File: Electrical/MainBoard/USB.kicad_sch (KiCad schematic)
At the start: 0 parts

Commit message: Add more schematics and begin floorplanning
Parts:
- added C10: 0.1 uF, Capacitor_SMD:C_0805_2012Metric_Pad1.18x1.45mm_HandSolder, symbol Device:C
- added D2 (x2): LED, LED_SMD:LED_0805_2012Metric_Pad1.15x1.40mm_HandSolder, symbol Device:LED
- added J13: USB_B_Micro, RobotLibrary:AMPHENOL_10118193-0001LF, symbol Connector:USB_B_Micro
- added R4 (x2): 130R, Resistor_SMD:R_0805_2012Metric_Pad1.20x1.40mm_HandSolder, symbol Device:R_US
- added U10: MCP2221A-I_SL, RobotLibrary:SOIC127P600X175-14N, symbol RobotLibary:MCP2221A-I_SL
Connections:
- new net: J13.2 (D-), U10.12 (D-)
- new net: J13.3 (D+), U10.13 (D+)
- new net: D2.1 (K), U10.2 (GP0)
- new net: D2.1 (K), U10.3 (GP1)
- new net: D2.2 (A), R4.2 (x2)
- new net +3.3V: C10.1, R4.1, R4.1, U10.1 (VDD), U10.11 (VUSB)
- new net GND: C10.2, J13.5 (GND), U10.14 (VSS)
- new net U1RX: U10.6 (UTX)
- new net U1TX: U10.5 (URX)
- new net USB Reset: U10.4 (~{RST})
- no-connect marks 0 -> 6
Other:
- note added: "RX Indicator"
- note added: "TX Indicator"

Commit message: Begin layout of pcb
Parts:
- renumbered U10 to U9
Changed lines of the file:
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@@
   (symbol (lib_id "power:GND") (at 173.355 135.89 0) (unit 1)
     (in_bom yes) (on_board yes) (dnp no) (fields_autoplaced)
-    (property "Reference" "#PWR0108" (at 173.355 142.24 0)
+    (property "Reference" "#PWR097" (at 173.355 142.24 0)
       (effects (font (size 1.27 1.27)) hide)
     )
@@
       (project "MainBoard"
         (path "/bd24c4db-4e36-4117-bd4f-5228ef241da9/f45a9536-5513-41e8-a632-51113262766c"
-          (reference "#PWR0108") (unit 1)
+          (reference "#PWR097") (unit 1)
         )
       )
@@
   (symbol (lib_id "power:GND") (at 238.125 136.525 0) (unit 1)
     (in_bom yes) (on_board yes) (dnp no) (fields_autoplaced)
-    (property "Reference" "#PWR0107" (at 238.125 142.875 0)
+    (property "Reference" "#PWR098" (at 238.125 142.875 0)
       (effects (font (size 1.27 1.27)) hide)
     )
@@
       (project "MainBoard"
         (path "/bd24c4db-4e36-4117-bd4f-5228ef241da9/f45a9536-5513-41e8-a632-51113262766c"
-          (reference "#PWR0107") (unit 1)
+          (reference "#PWR098") (unit 1)
         )
       )
@@
   (symbol (lib_id "power:GND") (at 247.015 104.14 0) (unit 1)
     (in_bom yes) (on_board yes) (dnp no)
-    (property "Reference" "#PWR0109" (at 247.015 110.49 0)
+    (property "Reference" "#PWR0100" (at 247.015 110.49 0)
       (effects (font (size 1.27 1.27)) hide)
     )
@@
       (project "MainBoard"
         (path "/bd24c4db-4e36-4117-bd4f-5228ef241da9/f45a9536-5513-41e8-a632-51113262766c"
-          (reference "#PWR0109") (unit 1)
+          (reference "#PWR0100") (unit 1)
         )
       )
@@
   (symbol (lib_id "RobotLibary:MCP2221A-I_SL") (at 222.885 121.285 0) (unit 1)
     (in_bom yes) (on_board yes) (dnp no) (fields_autoplaced)
-    (property "Reference" "U10" (at 222.885 99.06 0)
+    (property "Reference" "U9" (at 222.885 99.06 0)
       (effects (font (size 1.27 1.27)))
     )
@@
       (project "MainBoard"
         (path "/bd24c4db-4e36-4117-bd4f-5228ef241da9/f45a9536-5513-41e8-a632-51113262766c"
-          (reference "U10") (unit 1)
+          (reference "U9") (unit 1)
         )
       )
@@
   (symbol (lib_id "power:+3.3V") (at 273.05 114.3 0) (unit 1)
     (in_bom yes) (on_board yes) (dnp no) (fields_autoplaced)
-    (property "Reference" "#PWR0111" (at 273.05 118.11 0)
+    (property "Reference" "#PWR0101" (at 273.05 118.11 0)
       (effects (font (size 1.27 1.27)) hide)
     )
@@
       (project "MainBoard"
         (path "/bd24c4db-4e36-4117-bd4f-5228ef241da9/f45a9536-5513-41e8-a632-51113262766c"
-          (reference "#PWR0111") (unit 1)
+          (reference "#PWR0101") (unit 1)
         )
       )
@@
         )
         (path "/bd24c4db-4e36-4117-bd4f-5228ef241da9/f45a9536-5513-41e8-a632-51113262766c"
-          (reference "R25") (unit 1)
+          (reference "R15") (unit 1)
         )
       )
@@
   (symbol (lib_id "power:+3.3V") (at 288.925 237.49 0) (unit 1)
     (in_bom yes) (on_board yes) (dnp no) (fields_autoplaced)
-    (property "Reference" "#PWR048" (at 288.925 241.3 0)
+    (property "Reference" "#PWR0103" (at 288.925 241.3 0)
       (effects (font (size 1.27 1.27)) hide)
     )
@@
       (project "MainBoard"
         (path "/bd24c4db-4e36-4117-bd4f-5228ef241da9/f45a9536-5513-41e8-a632-51113262766c"
-          (reference "#PWR048") (unit 1)
+          (reference "#PWR0103") (unit 1)
         )
       )
@@
   (symbol (lib_id "power:+3.3V") (at 247.015 94.615 0) (unit 1)
     (in_bom yes) (on_board yes) (dnp no) (fields_autoplaced)
-    (property "Reference" "#PWR0110" (at 247.015 98.425 0)
+    (property "Reference" "#PWR099" (at 247.015 98.425 0)
       (effects (font (size 1.27 1.27)) hide)
     )
@@
       (project "MainBoard"
         (path "/bd24c4db-4e36-4117-bd4f-5228ef241da9/f45a9536-5513-41e8-a632-51113262766c"
-          (reference "#PWR0110") (unit 1)
+          (reference "#PWR099") (unit 1)
         )
       )
@@
   (symbol (lib_id "power:GND") (at 285.115 254.635 0) (unit 1)
     (in_bom yes) (on_board yes) (dnp no) (fields_autoplaced)
-    (property "Reference" "#PWR0106" (at 285.115 260.985 0)
+    (property "Reference" "#PWR0102" (at 285.115 260.985 0)
       (effects (font (size 1.27 1.27)) hide)
     )
@@
       (project "MainBoard"
         (path "/bd24c4db-4e36-4117-bd4f-5228ef241da9/f45a9536-5513-41e8-a632-51113262766c"
-          (reference "#PWR0106") (unit 1)
+          (reference "#PWR0102") (unit 1)
         )
       )
@@
         )
         (path "/bd24c4db-4e36-4117-bd4f-5228ef241da9/f45a9536-5513-41e8-a632-51113262766c"
-          (reference "C20") (unit 1)
+          (reference "C19") (unit 1)
         )
       )
@@
         )
         (path "/bd24c4db-4e36-4117-bd4f-5228ef241da9/f45a9536-5513-41e8-a632-51113262766c"
-          (reference "R26") (unit 1)
+          (reference "R16") (unit 1)
         )
       )
@@
         )
         (path "/bd24c4db-4e36-4117-bd4f-5228ef241da9/f45a9536-5513-41e8-a632-51113262766c"
-          (reference "J15") (unit 1)
-        )
-      )
+          (reference "J9") (unit 1)
+        )
+      )

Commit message: Add some finishing touches and create preliminary boms
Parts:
- removed D2 (x2): LED, LED_SMD:LED_0805_2012Metric_Pad1.15x1.40mm_HandSolder, symbol Device:LED
- added D1 (x2): LED, LED_SMD:LED_0805_2012Metric_Pad1.15x1.40mm_HandSolder, symbol Device:LED
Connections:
- net at U9.2 (GP0): now also D1.1 (K)
- net at U9.3 (GP1): now also D1.1 (K)
- net at R4.2: now also D1.2 (A) (x2)
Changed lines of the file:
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@@
-    )
-  )
-  (symbol (lib_id "Device:LED") (at 257.81 123.825 0) (unit 1)
-    (in_bom yes) (on_board yes) (dnp no)
-    (property "Reference" "D2" (at 259.08 126.365 0)
-      (effects (font (size 1.27 1.27)) (justify right))
-    )
-    (property "Value" "LED" (at 259.715 128.27 0)
-      (effects (font (size 1.27 1.27)) (justify right))
-    )
-    (property "Footprint" "LED_SMD:LED_0805_2012Metric_Pad1.15x1.40mm_HandSolder" (at 257.81 123.825 0)
-      (effects (font (size 1.27 1.27)) hide)
-    )
-    (property "Datasheet" "https://www.we-online.com/katalog/datasheet/150080RS75000.pdf" (at 257.81 123.825 0)
-      (effects (font (size 1.27 1.27)) hide)
-    )
-    (property "Description" "LED GREEN CLEAR 0805 SMD" (at 257.81 123.825 0)
-      (effects (font (size 1.27 1.27)) hide)
-    )
-    (property "Mfr" "Würth Elektronik" (at 257.81 123.825 0)
-      (effects (font (size 1.27 1.27)) hide)
-    )
-    (property "Mfr P/N" "150080VS75000" (at 257.81 123.825 0)
-      (effects (font (size 1.27 1.27)) hide)
-    )
-    (property "Supplier 1" "DigiKey" (at 257.81 123.825 0)
-      (effects (font (size 1.27 1.27)) hide)
-    )
-    (property "Supplier 1 P/N" "732-4986-1-ND" (at 257.81 123.825 0)
-      (effects (font (size 1.27 1.27)) hide)
-    )
-    (property "Supplier 2" "" (at 257.81 123.825 0)
-      (effects (font (size 1.27 1.27)) hide)
-    )
-    (property "Supplier 2 P/N" "" (at 257.81 123.825 0)
-      (effects (font (size 1.27 1.27)) hide)
-    )
-    (pin "1")
-    (pin "2")
-    (instances
-      (project "MainBoard"
-        (path "/bd24c4db-4e36-4117-bd4f-5228ef241da9/783fabe8-20be-46c9-9aa7-e8ec2689d507"
-          (reference "D2") (unit 1)
-        )
-        (path "/bd24c4db-4e36-4117-bd4f-5228ef241da9/f45a9536-5513-41e8-a632-51113262766c"
-          (reference "D9") (unit 1)
-        )
-      )
     )
   )
@@
     )
   )
-  (symbol (lib_id "Device:LED") (at 258.445 120.015 0) (unit 1)
-    (in_bom yes) (on_board yes) (dnp no)
-    (property "Reference" "D2" (at 260.35 115.57 0)
-      (effects (font (size 1.27 1.27)) (justify right))
-    )
-    (property "Value" "LED" (at 260.35 117.475 0)
-      (effects (font (size 1.27 1.27)) (justify right))
-    )
-    (property "Footprint" "LED_SMD:LED_0805_2012Metric_Pad1.15x1.40mm_HandSolder" (at 258.445 120.015 0)
-      (effects (font (size 1.27 1.27)) hide)
-    )
-    (property "Datasheet" "https://www.we-online.com/katalog/datasheet/150080RS75000.pdf" (at 258.445 120.015 0)
-      (effects (font (size 1.27 1.27)) hide)
-    )
-    (property "Description" "LED GREEN CLEAR 0805 SMD" (at 258.445 120.015 0)
-      (effects (font (size 1.27 1.27)) hide)
-    )
-    (property "Mfr" "Würth Elektronik" (at 258.445 120.015 0)
-      (effects (font (size 1.27 1.27)) hide)
-    )
-    (property "Mfr P/N" "150080VS75000" (at 258.445 120.015 0)
-      (effects (font (size 1.27 1.27)) hide)
-    )
-    (property "Supplier 1" "DigiKey" (at 258.445 120.015 0)
-      (effects (font (size 1.27 1.27)) hide)
-    )
-    (property "Supplier 1 P/N" "732-4986-1-ND" (at 258.445 120.015 0)
-      (effects (font (size 1.27 1.27)) hide)
-    )
-    (property "Supplier 2" "" (at 258.445 120.015 0)
-      (effects (font (size 1.27 1.27)) hide)
-    )
-    (property "Supplier 2 P/N" "" (at 258.445 120.015 0)
-      (effects (font (size 1.27 1.27)) hide)
-    )
-    (pin "1")
-    (pin "2")
-    (instances
-      (project "MainBoard"
-        (path "/bd24c4db-4e36-4117-bd4f-5228ef241da9/783fabe8-20be-46c9-9aa7-e8ec2689d507"
-          (reference "D2") (unit 1)
-        )
-        (path "/bd24c4db-4e36-4117-bd4f-5228ef241da9/f45a9536-5513-41e8-a632-51113262766c"
-          (reference "D10") (unit 1)
-        )
-      )
-    )
-  )
   (symbol (lib_id "power:+3.3V") (at 247.015 94.615 0) (unit 1)
     (in_bom yes) (on_board yes) (dnp no) (fields_autoplaced)
@@
         )
       )
+    )
+  )
+  (symbol (lib_id "Device:LED") (at 258.445 120.015 0) (unit 1)
+    (in_bom yes) (on_board yes) (dnp no)
+    (property "Reference" "D1" (at 259.715 116.84 0)
+      (effects (font (size 1.27 1.27)) (justify right))
+    )
+    (property "Value" "LED" (at 259.715 114.935 0)
+      (effects (font (size 1.27 1.27)) (justify right))
+    )
+    (property "Footprint" "LED_SMD:LED_0805_2012Metric_Pad1.15x1.40mm_HandSolder" (at 258.445 120.015 0)
+      (effects (font (size 1.27 1.27)) hide)
+    )
+    (property "Datasheet" "https://www.we-online.com/katalog/datasheet/150080RS75000.pdf" (at 258.445 120.015 0)
+      (effects (font (size 1.27 1.27)) hide)
+    )
+    (property "Description" "LED RED CLEAR 0805 SMD" (at 258.445 120.015 0)
+      (effects (font (size 1.27 1.27)) hide)
+    )
+    (property "Mfr" "Würth Elektronik" (at 258.445 120.015 0)
+      (effects (font (size 1.27 1.27)) hide)
+    )
+    (property "Mfr P/N" "150080RS75000" (at 258.445 120.015 0)
+      (effects (font (size 1.27 1.27)) hide)
+    )
+    (property "Supplier 1" "DigiKey" (at 258.445 120.015 0)
+      (effects (font (size 1.27 1.27)) hide)
+    )
+    (property "Supplier 1 P/N" "732-4984-1-ND" (at 258.445 120.015 0)
+      (effects (font (size 1.27 1.27)) hide)
+    )
+    (property "Supplier 2" "" (at 258.445 120.015 0)
+      (effects (font (size 1.27 1.27)) hide)
+    )
+    (property "Supplier 2 P/N" "" (at 258.445 120.015 0)
+      (effects (font (size 1.27 1.27)) hide)
+    )
+    (pin "1")
+    (pin "2")
+    (instances
+      (project "MainBoard"
+        (path "/bd24c4db-4e36-4117-bd4f-5228ef241da9/783fabe8-20be-46c9-9aa7-e8ec2689d507"
+          (reference "D1") (unit 1)
+        )
+        (path "/bd24c4db-4e36-4117-bd4f-5228ef241da9/8ba935aa-d6da-451b-8954-3c3ef7086bfd"
+          (reference "D1") (unit 1)
+        )
+        (path "/bd24c4db-4e36-4117-bd4f-5228ef241da9/f45a9536-5513-41e8-a632-51113262766c"
+          (reference "D10") (unit 1)
+        )
+      )
+    )
+  )
+  (symbol (lib_id "Device:LED") (at 257.81 123.825 0) (unit 1)
+    (in_bom yes) (on_board yes) (dnp no)
+    (property "Reference" "D1" (at 259.715 128.27 0)
+      (effects (font (size 1.27 1.27)) (justify right))
+    )
+    (property "Value" "LED" (at 259.715 126.365 0)
+      (effects (font (size 1.27 1.27)) (justify right))
+    )
+    (property "Footprint" "LED_SMD:LED_0805_2012Metric_Pad1.15x1.40mm_HandSolder" (at 257.81 123.825 0)
+      (effects (font (size 1.27 1.27)) hide)
+    )
+    (property "Datasheet" "https://www.we-online.com/katalog/datasheet/150080RS75000.pdf" (at 257.81 123.825 0)
+      (effects (font (size 1.27 1.27)) hide)
+    )
+    (property "Description" "LED RED CLEAR 0805 SMD" (at 257.81 123.825 0)
+      (effects (font (size 1.27 1.27)) hide)
+    )
+    (property "Mfr" "Würth Elektronik" (at 257.81 123.825 0)
+      (effects (font (size 1.27 1.27)) hide)
+    )
+    (property "Mfr P/N" "150080RS75000" (at 257.81 123.825 0)
+      (effects (font (size 1.27 1.27)) hide)
+    )
+    (property "Supplier 1" "DigiKey" (at 257.81 123.825 0)
+      (effects (font (size 1.27 1.27)) hide)
+    )
+    (property "Supplier 1 P/N" "732-4984-1-ND" (at 257.81 123.825 0)
+      (effects (font (size 1.27 1.27)) hide)
+    )
+    (property "Supplier 2" "" (at 257.81 123.825 0)
+      (effects (font (size 1.27 1.27)) hide)
+    )
+    (property "Supplier 2 P/N" "" (at 257.81 123.825 0)
+      (effects (font (size 1.27 1.27)) hide)
+    )
+    (pin "1")
+    (pin "2")
+    (instances
+      (project "MainBoard"
+        (path "/bd24c4db-4e36-4117-bd4f-5228ef241da9/783fabe8-20be-46c9-9aa7-e8ec2689d507"
+          (reference "D1") (unit 1)
+        )
+        (path "/bd24c4db-4e36-4117-bd4f-5228ef241da9/8ba935aa-d6da-451b-8954-3c3ef7086bfd"
+          (reference "D1") (unit 1)
+        )
+        (path "/bd24c4db-4e36-4117-bd4f-5228ef241da9/f45a9536-5513-41e8-a632-51113262766c"
+          (reference "D9") (unit 1)
+        )
+      )

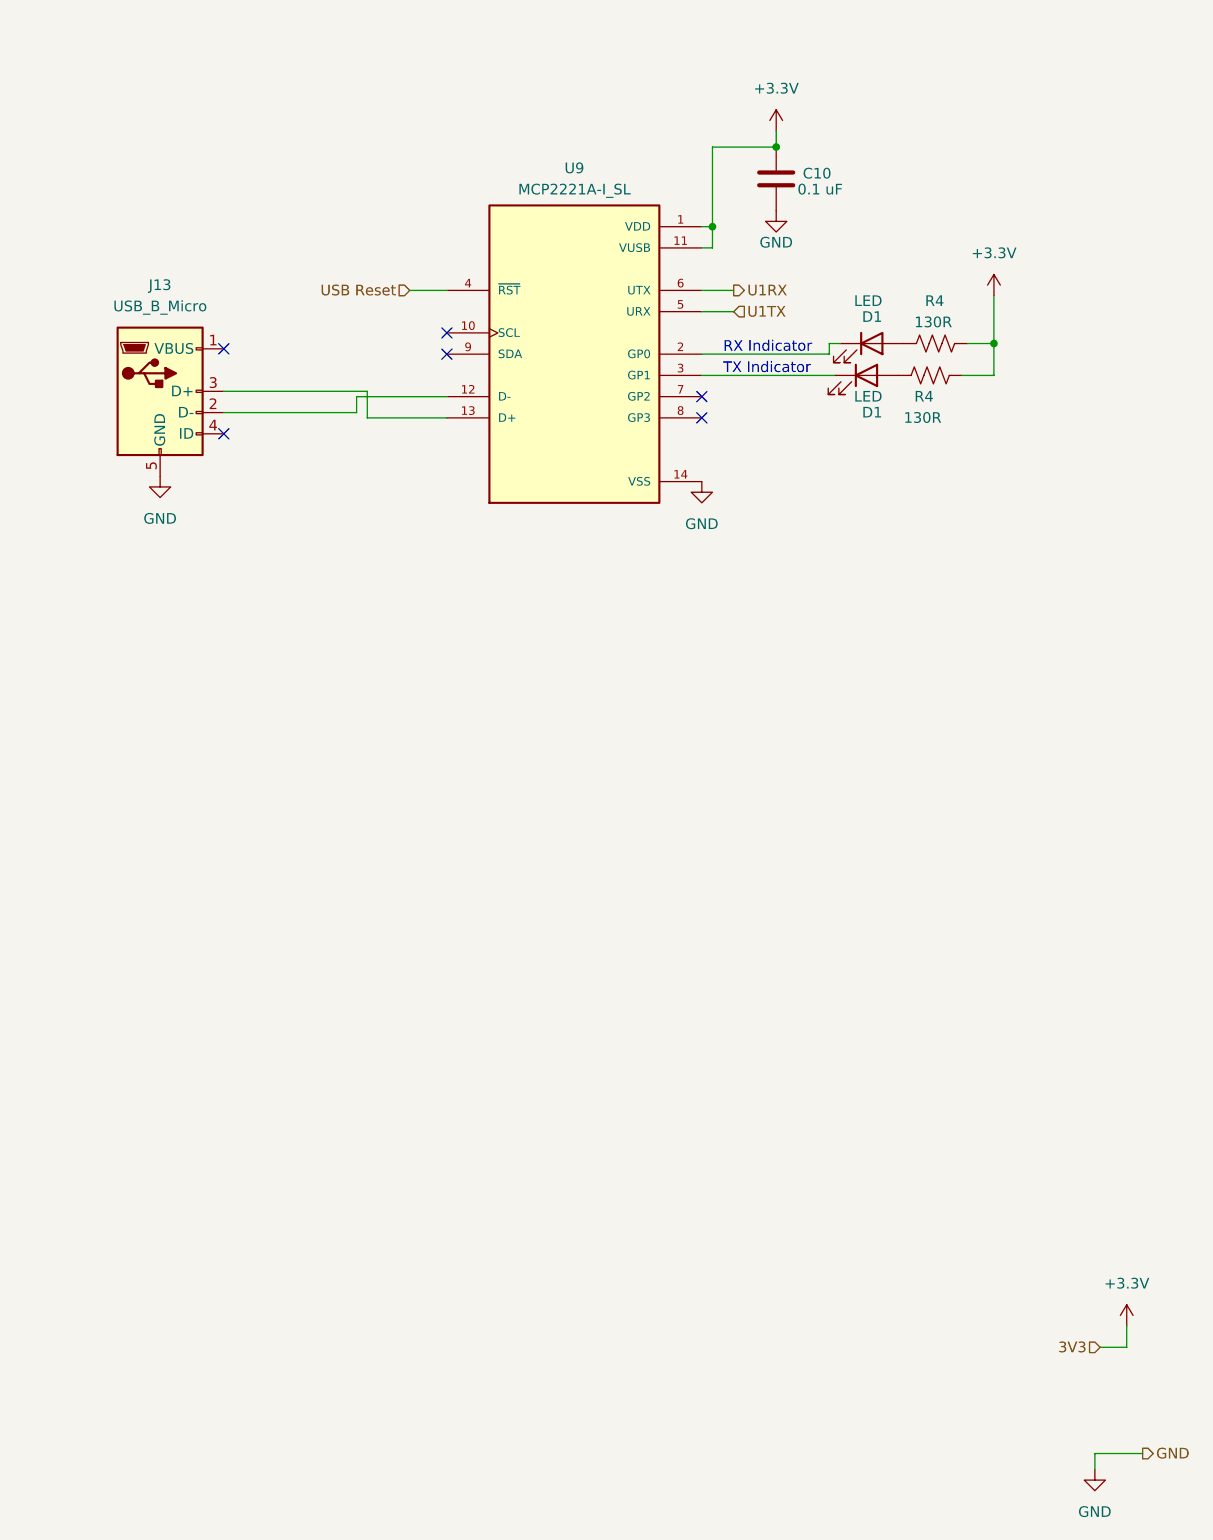
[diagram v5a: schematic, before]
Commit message: Fix SPI3 and make visual improvements
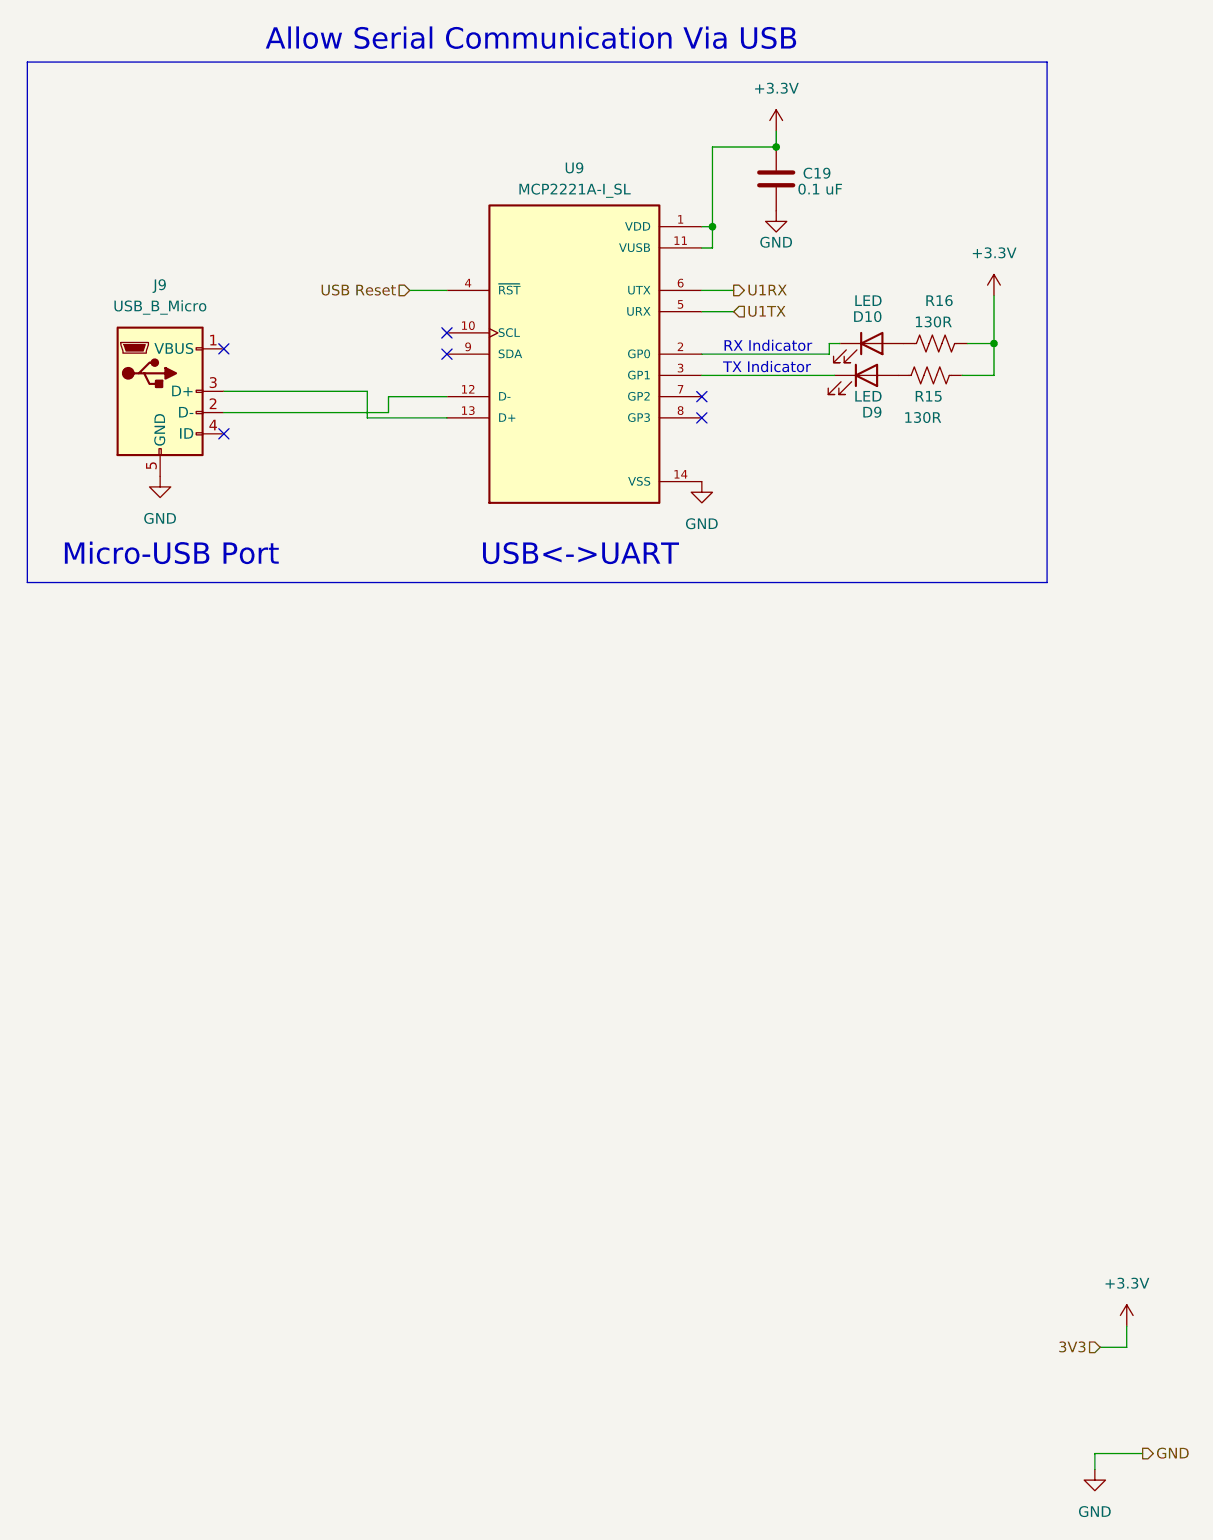
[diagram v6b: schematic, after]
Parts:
- renumbered C10 to C19, D1 to D10, D1 to D9, J13 to J9, R4 to R15, R4 to R16
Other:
- note added: "Allow Serial Communication Via USB"
- note added: "Micro-USB Port"
- note added: "USB<->UART"
